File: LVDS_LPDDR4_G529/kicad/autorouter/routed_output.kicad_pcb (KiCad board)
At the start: 10 copper layers, 200 x 125 mm, 8 parts, among them IC1 ADC12DL500ACF_Aligned, U1 MT53D512M16D1DS_Aligned, U2 FT601Q_Aligned, U3 Ti90G529_Functions

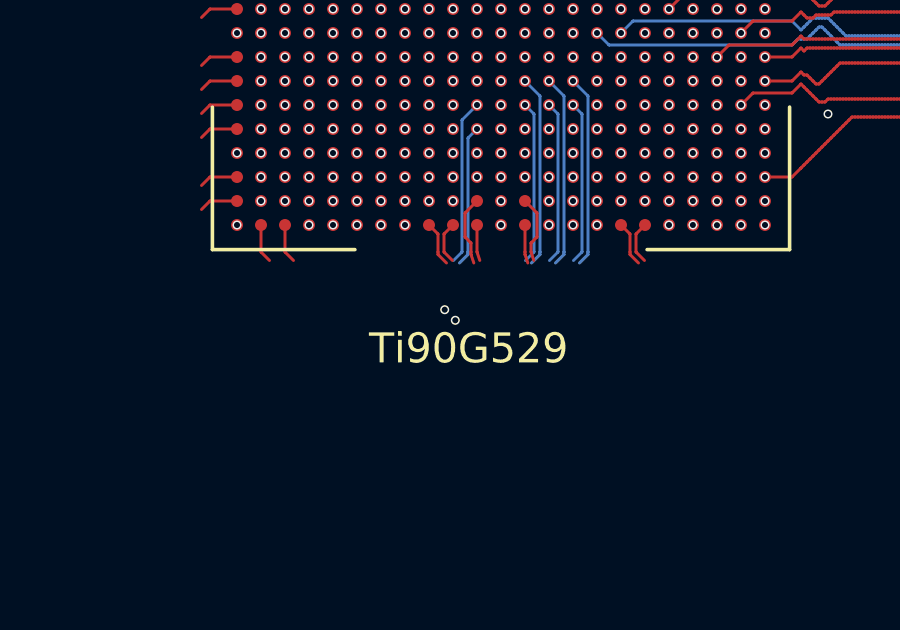
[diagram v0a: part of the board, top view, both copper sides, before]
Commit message: remove existing lvds track
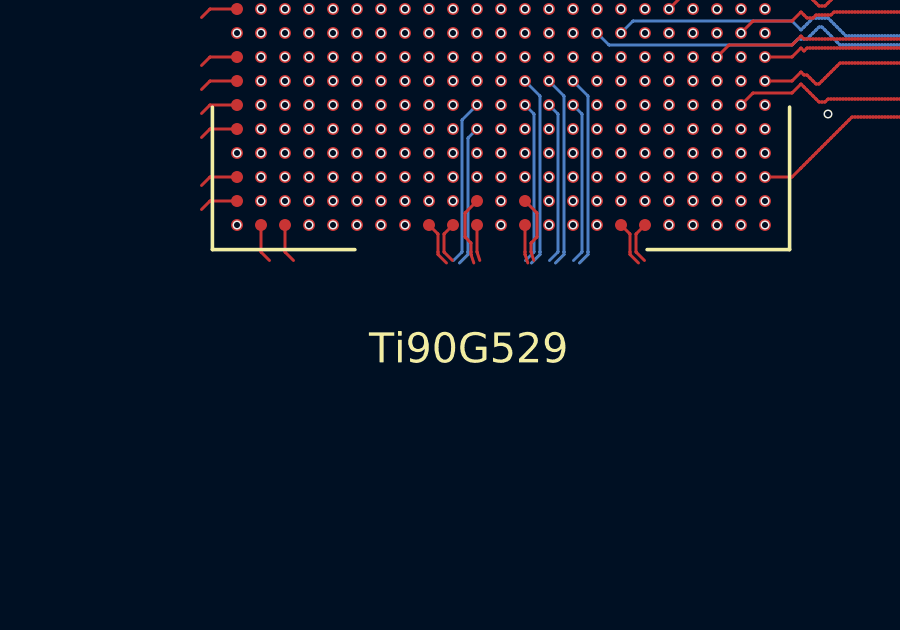
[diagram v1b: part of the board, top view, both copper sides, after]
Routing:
- net /fpga_adc/lvds_rx1_8_P: track 64.0 -> 6.43 mm, vias 3 -> 2
- net /fpga_adc/lvds_rx1_8_N: track 62.1 -> 5.54 mm, vias 3 -> 2
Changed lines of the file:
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@@
 	)
 	(via
-		(at 193.876777 114.976777)
+		(at 194.6 109.4)
 		(size 0.3)
 		(drill 0.2)
@@
 	)
 	(via
-		(at 194.6 109.4)
-		(size 0.3)
-		(drill 0.2)
-		(layers "F.Cu" "B.Cu")
-		(net 780)
-	)
-	(via
 		(at 146.5 109)
 		(size 0.3)
 		(drill 0.2)
 		(layers "F.Cu" "B.Cu")
-		(net 780)
-	)
-	(segment
-		(start 193.657574 114.976777)
-		(end 193.876777 114.976777)
-		(width 0.1)
-		(layer "In1.Cu")
-		(net 780)
-	)
-	(segment
-		(start 147.017851 111.436396)
-		(end 157.876455 122.295)
-		(width 0.1)
-		(layer "In1.Cu")
 		(net 780)
 	)
@@
 	)
 	(segment
-		(start 157.876455 122.295)
-		(end 186.339351 122.295)
-		(width 0.1)
-		(layer "In1.Cu")
-		(net 780)
-	)
-	(segment
-		(start 186.339351 122.295)
-		(end 193.657574 114.976777)
-		(width 0.1)
-		(layer "In1.Cu")
-		(net 780)
-	)
-	(segment
-		(start 193.876777 114.976777)
-		(end 193.249497 114.976777)
-		(width 0.09)
-		(layer "In2.Cu")
-		(net 780)
-	)
-	(segment
-		(start 194.005719 112.982843)
-		(end 193.989877 112.982843)
-		(width 0.1)
-		(layer "In2.Cu")
-		(net 780)
-	)
-	(segment
 		(start 194.1 112.7)
 		(end 194.005719 112.982843)
@@
 		(net 780)
 	)
-	(segment
-		(start 192.91 114.06272)
-		(end 193.13636 113.83636)
-		(width 0.09)
-		(layer "In2.Cu")
-		(net 780)
-	)
-	(segment
-		(start 193.249497 114.976777)
-		(end 192.91 114.63728)
-		(width 0.09)
-		(layer "In2.Cu")
-		(net 780)
-	)
-	(segment
-		(start 192.91 114.63728)
-		(end 192.91 114.06272)
-		(width 0.09)
-		(layer "In2.Cu")
-		(net 780)
-	)
-	(segment
-		(start 193.989877 112.982843)
-		(end 193.13636 113.83636)
-		(width 0.1)
-		(layer "In2.Cu")
-		(net 780)
-	)
 	(via
 		(at 151.5 108)
@@
 		(net 807)
 	)
-	(via
-		(at 193.523223 114.623223)
-		(size 0.3)
-		(drill 0.2)
-		(layers "F.Cu" "B.Cu")
-		(net 807)
-	)
-	(segment
-		(start 157.969298 122.105)
-		(end 186.260649 122.105)
-		(width 0.1)
-		(layer "In1.Cu")
-		(net 807)
-	)
 	(segment
 		(start 147.5 109)
@@
 	)
 	(segment
-		(start 186.260649 122.105)
-		(end 193.523223 114.842426)
-		(width 0.1)
-		(layer "In1.Cu")
-		(net 807)
-	)
-	(segment
-		(start 193.523223 114.842426)
-		(end 193.523223 114.623223)
-		(width 0.1)
-		(layer "In1.Cu")
-		(net 807)
-	)
-	(segment
-		(start 147.217851 111.353553)
-		(end 157.969298 122.105)
-		(width 0.1)
-		(layer "In1.Cu")
-		(net 807)
-	)
-	(segment
 		(start 147.1 111)
 		(end 147.217851 111.353553)
@@
 	)
 	(segment
-		(start 194.205719 113.128631)
-		(end 193.103535 114.230815)
-		(width 0.1)
-		(layer "In2.Cu")
-		(net 807)
-	)
-	(segment
-		(start 193.523223 114.623223)
-		(end 193.349669 114.796777)
-		(width 0.09)
-		(layer "In2.Cu")
-		(net 807)
-	)
-	(segment
-		(start 193.324057 114.796777)
-		(end 193.09 114.56272)
-		(width 0.09)
-		(layer "In2.Cu")
-		(net 807)
-	)
-	(segment
 		(start 194.6 110.2)
 		(end 194.3 110.5)
@@
 		(width 0.1)
 		(layer "In2.Cu")
-		(net 807)
-	)
-	(segment
-		(start 193.349669 114.796777)
-		(end 193.324057 114.796777)
-		(width 0.09)
-		(layer "In2.Cu")
-		(net 807)
-	)
-	(segment
-		(start 194.205719 113.065685)
-		(end 194.205719 113.128631)
-		(width 0.1)
-		(layer "In2.Cu")
-		(net 807)
-	)
-	(segment
-		(start 193.103535 114.230815)
-		(end 193.103535 114.569185)
-		(width 0.1)
-		(layer "In2.Cu")
